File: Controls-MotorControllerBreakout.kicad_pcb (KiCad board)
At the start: 2 copper layers, 47.8 x 44.5 mm, 38 parts, among them J1 MC CAN 1, J2 MC CAN 2, J3 CTRLS, J4 EXT PWR, J5 CANDAPTER, Q1 PMV35EPER, U1 TPS2121RUXR

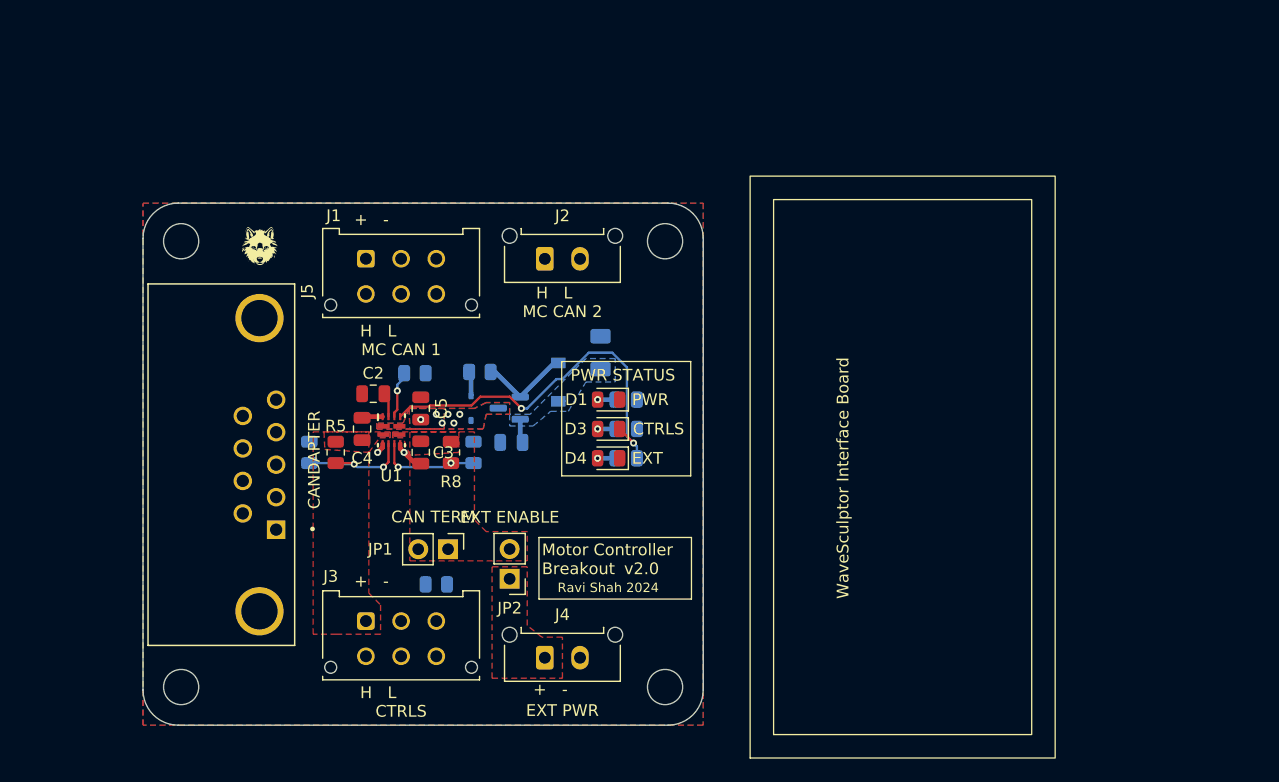
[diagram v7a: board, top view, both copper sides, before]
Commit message: better output/CAN routing + testpoints
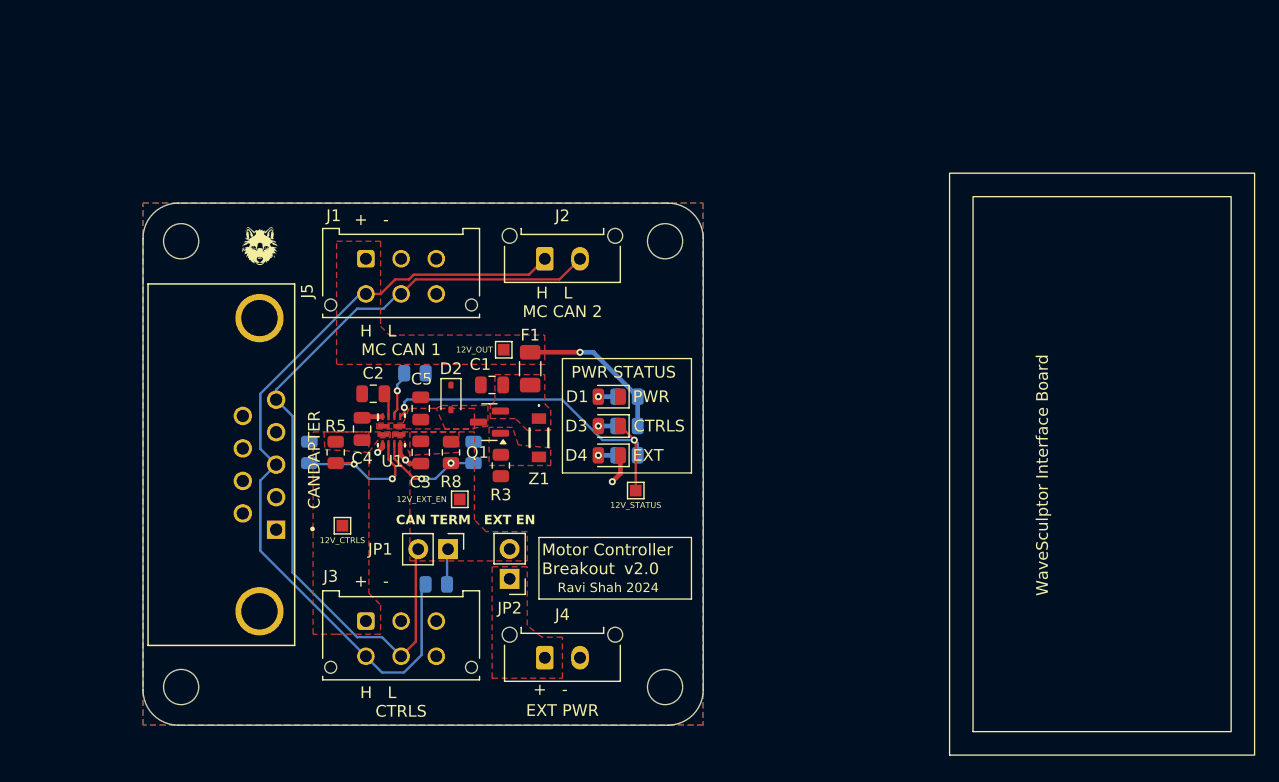
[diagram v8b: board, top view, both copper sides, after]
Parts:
- added TP1: 12V_EXT_EN, TestPoint:TestPoint_Pad_1.0x1.0mm, F.Cu at (99.5, 69.2)
- added TP2: 12V_CTRLS, TestPoint:TestPoint_Pad_1.0x1.0mm, F.Cu at (89.5, 71.5)
- added TP4: 12V_OUT, TestPoint:TestPoint_Pad_1.0x1.0mm, F.Cu at (103.2, 56.5)
- added TP5: 12V_STATUS, TestPoint:TestPoint_Pad_1.0x1.0mm, F.Cu at (114.5, 68.5)
- C1, D2, F1, Q1, R3, Z1: moved to F.Cu
- JP2: value EXT ENABLE -> EXT EN
- moved LOGO2 17.0 mm to (154.2, 66.2)
- moved R3 8.17 mm to (103.0, 66.4), turned to 90 degrees
- moved F1 6.15 mm to (105.5, 58.1)
- moved C1 5.17 mm to (102.2, 59.5)
- moved Z1 5.02 mm to (106.2, 64.0), turned to -90 degrees
- moved Q1 2.06 mm to (102.0, 62.7)
- moved D2 1.94 mm to (98.8, 60.6)
- moved D1 0.26 mm to (112.2, 60.5)
- moved D3 0.26 mm to (112.2, 63.0)
- moved D4 0.26 mm to (112.2, 65.5)
- moved R10 0.26 mm to (113.8, 65.5)
- moved R2 0.26 mm to (113.8, 60.5)
- moved R9 0.26 mm to (113.8, 63.0)
- moved LOGO1 0.25 mm to (76.2, 66.0)
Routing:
- net /CAN_L: track 0.66 -> 68.6 mm
- net /CAN_H: track 0.37 -> 68.3 mm
- net +12V: track 0.00 -> 13.2 mm, vias 0 -> 1
- net Net-(Q1-G): track 7.86 -> 0.00 mm
- net Net-(Q1-S): track 2.91 -> 0.00 mm
- net /+12V_STATUS: track 32.7 -> 30.0 mm
- net Net-(JP1-A): track 0.34 -> 3.04 mm
- net /PowerDist/OV2: track 10.3 -> 12.6 mm
- net /PowerDist/OV1: track 8.70 -> 9.30 mm
- net GND: track 8.67 -> 8.26 mm, vias 2 -> 3
- net /PowerDist/+12V_SEL: vias 6 -> 0
- added copper zone on F.Cu, net +12V
- added copper zone on F.Cu, net Net-(Q1-G)
- added copper zone on F.Cu, net Net-(Q1-S)
- removed copper zone on B.Cu, net /PowerDist/+12V_SEL
- removed copper zone on B.Cu, net Net-(Q1-S)
